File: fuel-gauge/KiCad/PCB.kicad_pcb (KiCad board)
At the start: 2 copper layers, 100 x 70 mm, 39 parts, among them P1 CONN_01X04, P2 CONN_01X04, P3 CONN_01X04, Q1 BSS84, Q2 BSS138, Q3 2N7002, SW1 Switch_SPDT_x2, U1 AQV252G, U2 SN74LVC1G08DBVR, U3 TLV3691IDCKR, U4 bq34z100pw

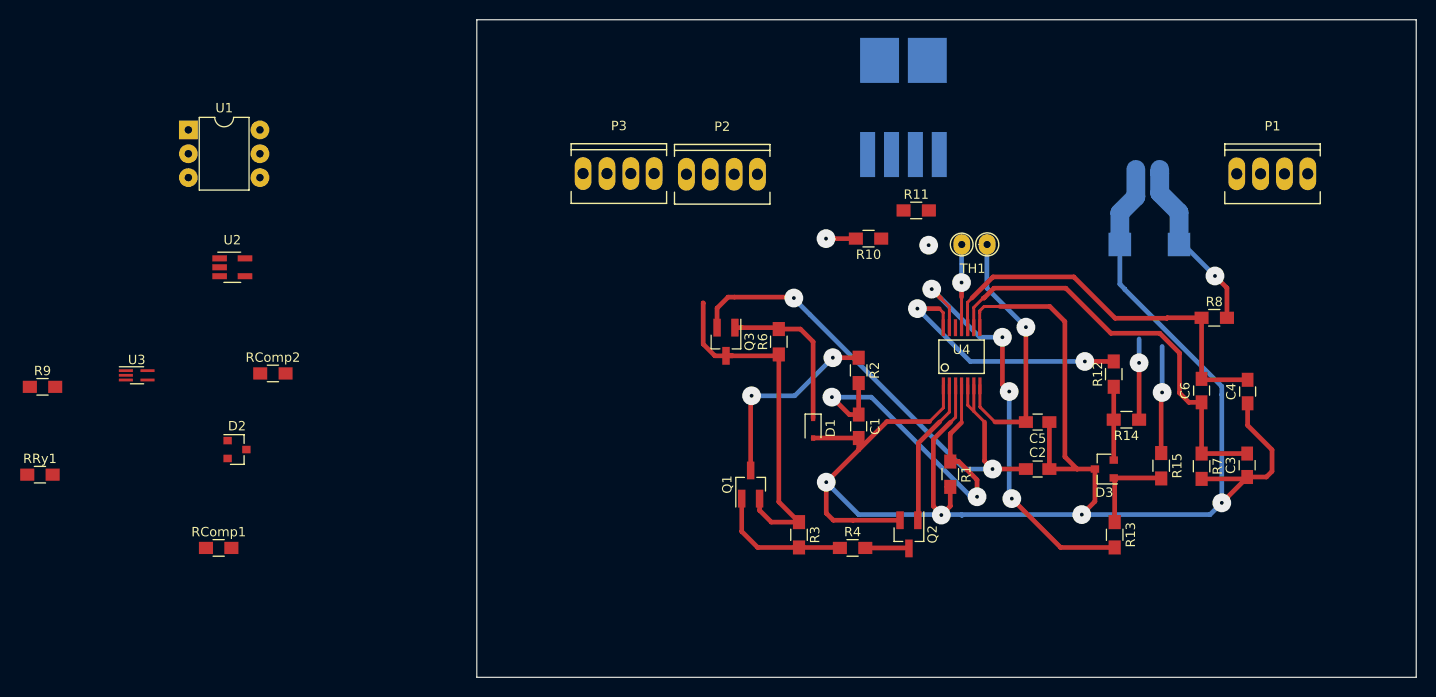
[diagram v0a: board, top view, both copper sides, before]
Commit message: Update fuel gauge pcb design to the v2
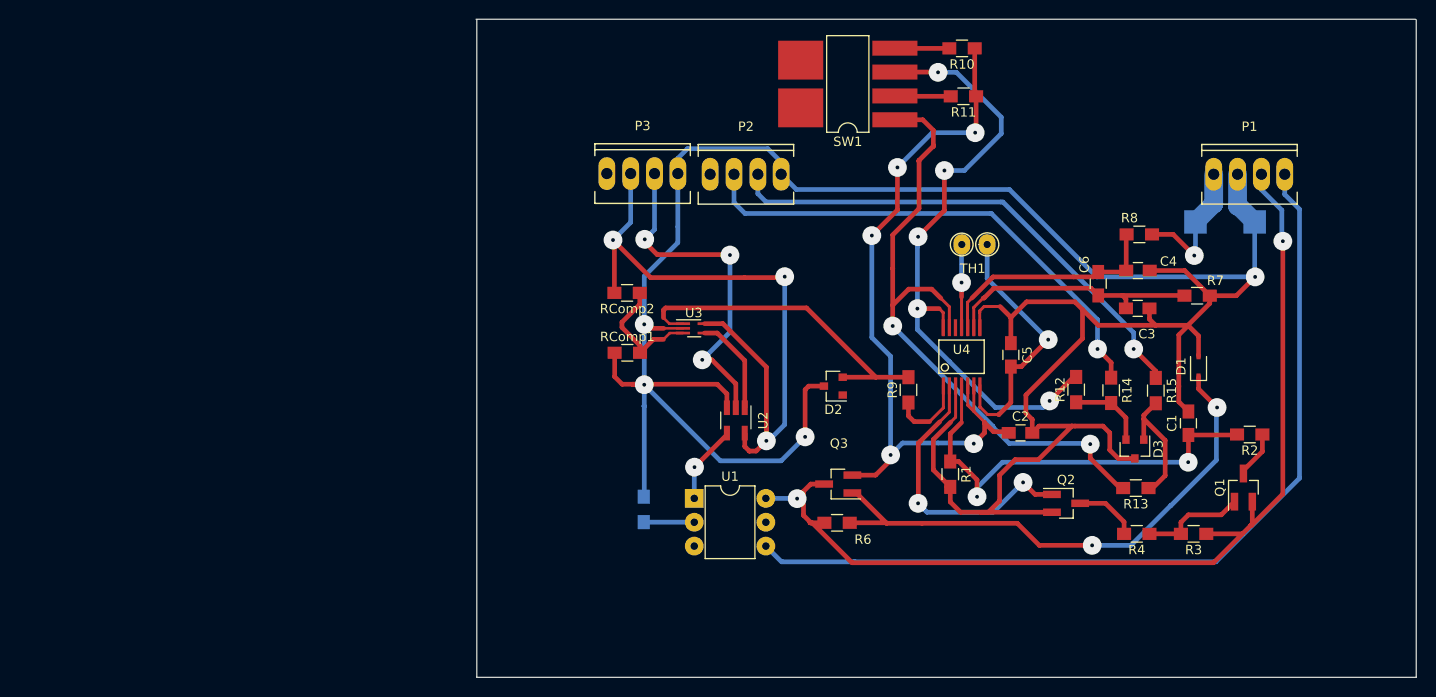
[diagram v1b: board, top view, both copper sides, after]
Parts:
- RRy1: moved to B.Cu
- SW1: moved to F.Cu
- moved R9 92.2 mm to (145.9, 99.4), turned to 90 degrees
- moved U1 66.6 mm to (123.2, 111.0)
- moved RRy1 64.4 mm to (117.8, 112.1), turned to 270 degrees
- moved D2 63.8 mm to (137.9, 99.0), turned to 180 degrees
- moved U3 59.5 mm to (123.1, 93.1)
- moved U2 56.0 mm to (127.6, 102.7), turned to 270 degrees
- moved Q1 52.5 mm to (181.6, 109.8)
- moved RComp1 48.2 mm to (116.0, 95.5)
- moved R2 42.2 mm to (182.3, 104.2), turned to 180 degrees
- moved R3 42.0 mm to (176.3, 114.7), turned to 180 degrees
- moved D1 41.5 mm to (176.8, 96.9), turned to 90 degrees
- moved RComp2 38.7 mm to (116.0, 89.1), turned to 180 degrees
- moved C1 35.1 mm to (175.8, 103.0), turned to 90 degrees
- moved R4 30.3 mm to (170.2, 114.7), turned to 180 degrees
- moved R10 22.6 mm to (151.7, 63.0)
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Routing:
- net GNDREF: track 92.3 -> 302.6 mm, vias 0 -> 4
- net Net-(R9-Pad1): track 112.2 -> 8.58 mm, vias 4 -> 0
- net /PUSHBUTTON: track 0.00 -> 94.3 mm
- net +5V: track 0.00 -> 73.1 mm, vias 0 -> 3
- net /BATT+: track 38.4 -> 110.2 mm, vias 0 -> 2
- net /SDA: track 8.80 -> 53.6 mm
- net /SCL: track 11.6 -> 54.0 mm
- net Net-(D1-Pad1): track 17.1 -> 58.6 mm, vias 0 -> 2
- net Net-(R12-Pad2): track 28.5 -> 67.9 mm, vias 2 -> 5
- net Net-(P3-Pad3): track 0.00 -> 36.9 mm, vias 0 -> 3
- net Net-(D2-Pad1): track 0.00 -> 35.9 mm
- net Net-(R13-Pad2): track 45.9 -> 70.3 mm, vias 4 -> 2
- net REG_IN: track 56.2 -> 79.5 mm, vias 2 -> 5
- net Net-(C3-Pad2): track 45.9 -> 28.1 mm
- net Net-(C4-Pad2): track 43.0 -> 25.7 mm
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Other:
- board size 100 x 70 mm -> 100.1 x 70 mm
- rule trace_min: 0.32 -> 0.28

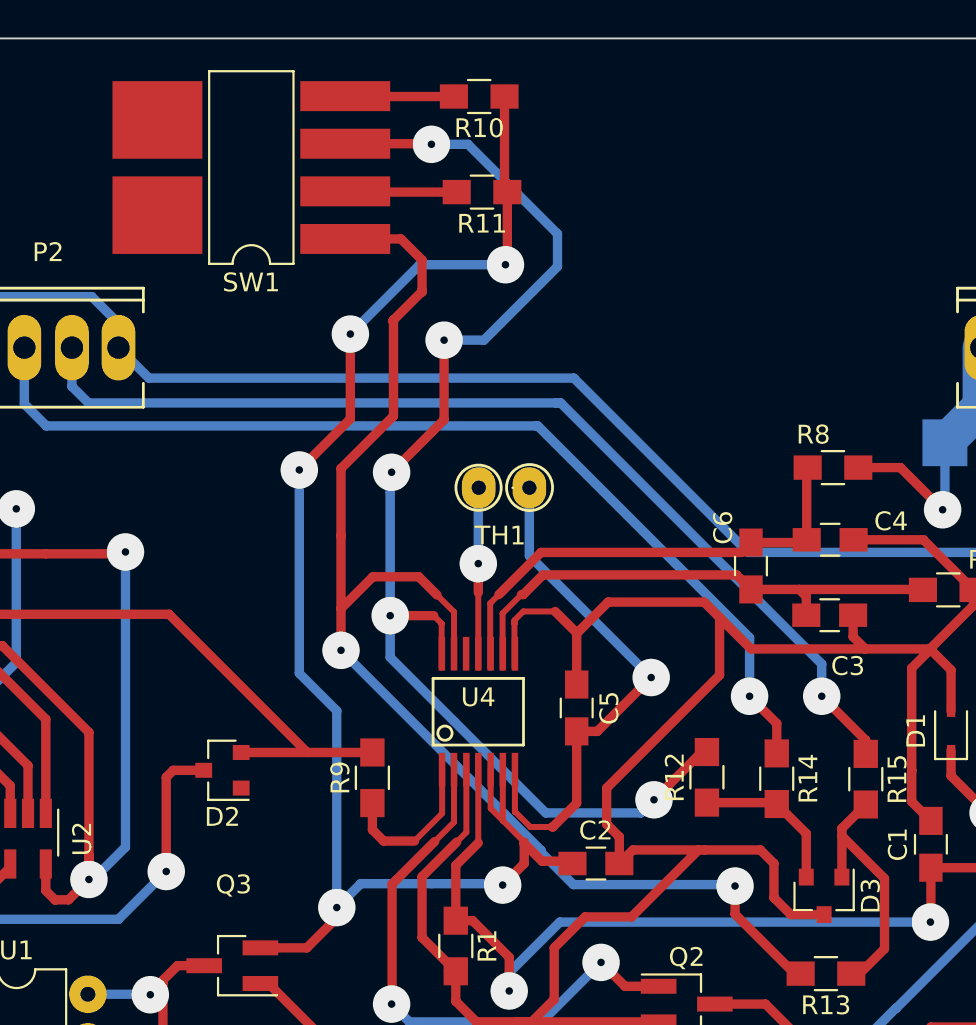
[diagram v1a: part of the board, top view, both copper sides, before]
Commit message: Switch moved because of the proximity to the connector.
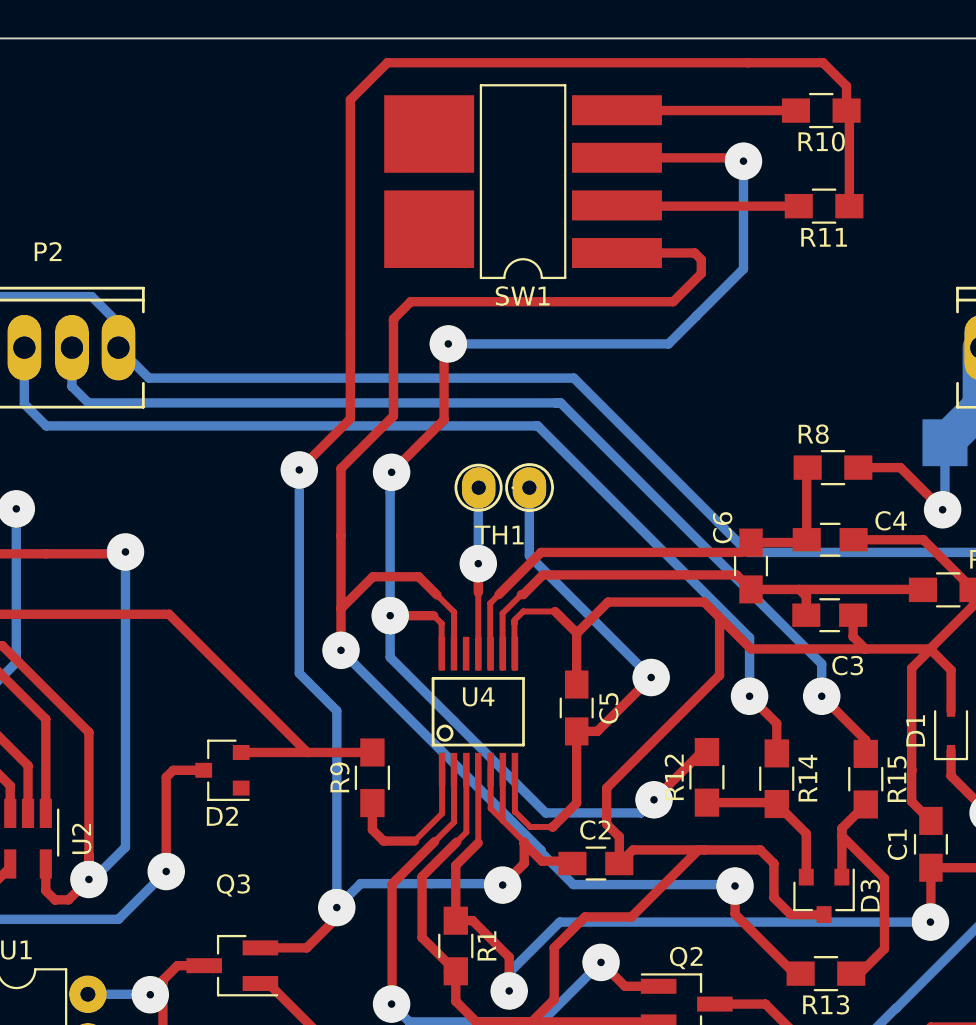
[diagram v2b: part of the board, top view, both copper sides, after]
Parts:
- moved R10 18.3 mm to (169.9, 63.8)
- moved R11 18.3 mm to (170.1, 68.9)
- moved SW1 14.5 mm to (157.8, 71.4)
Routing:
- net REG_IN: track 79.5 -> 107.8 mm, vias 5 -> 3
- net Net-(R13-Pad2): track 70.3 -> 84.6 mm
- net Net-(R12-Pad2): track 67.9 -> 75.0 mm
- net Net-(R11-Pad2): track 5.97 -> 9.77 mm
- net Net-(R10-Pad2): track 5.81 -> 9.59 mm
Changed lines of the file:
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@@
-(kicad_pcb (version 4) (host pcbnew 4.0.0-rc2-stable)
+(kicad_pcb (version 4) (host pcbnew 4.0.6)
   (general
     (links 76)
     (no_connects 0)
-    (area 94.899999 49.899999 218.428572 144.700001)
+    (area 99.874999 59.899999 200.050001 130.050001)
     (thickness 1.6)
     (drawings 17)
-    (tracks 457)
+    (tracks 460)
     (zones 0)
     (modules 39)
@@
   )
   (module myfootprint:R_0805_My_HandSoldering (layer F.Cu)
-    (at 151.65 63.05 180)
+    (at 169.9 63.8 180)
     (descr "Resistor SMD 0805, hand soldering")
     (tags "resistor 0805")
@@
   )
   (module myfootprint:R_0805_My_HandSoldering (layer F.Cu)
-    (at 151.8 68.15 180)
+    (at 170.05 68.9 180)
     (descr "Resistor SMD 0805, hand soldering")
     (tags "resistor 0805")
@@
   )
   (module footprint:SW1-DIP-8-_6_Handsoldering (layer F.Cu)
-    (at 143.3 70.65 180)
+    (at 157.8 71.4 180)
     (descr "8-lead though-hole mounted DIP package, row spacing 7.62 mm (300 mils), LongPads")
     (tags "THT DIP DIL PDIP 2.54mm 7.62mm 300mil LongPads")
@@
   (segment (start 150.4 104.075) (end 151.6 102.875) (width 0.5) (layer F.Cu) (net 1))
   (segment (start 150.4 107.025) (end 150.4 107.025) (width 0.5) (layer F.Cu) (net 1) (status 30))
+  (segment (start 171.4 68.9) (end 171.4 63.95) (width 0.5) (layer F.Cu) (net 2) (status C00000))
+  (segment (start 171.4 63.95) (end 171.25 63.8) (width 0.5) (layer F.Cu) (net 2) (status C00000))
+  (segment (start 166 61.25) (end 170 61.25) (width 0.5) (layer F.Cu) (net 2))
+  (segment (start 144.775 63.225) (end 146.75 61.25) (width 0.5) (layer F.Cu) (net 2))
+  (segment (start 146.75 61.25) (end 166 61.25) (width 0.5) (layer F.Cu) (net 2))
   (segment (start 144.775 75.725) (end 144.775 80.25) (width 0.5) (layer F.Cu) (net 2))
-  (segment (start 144.05 95.825) (end 144.05 106.325) (width 0.5) (layer B.Cu) (net 2))
+  (segment (start 144.05 106.325) (end 144.05 95.825) (width 0.5) (layer B.Cu) (net 2))
   (via (at 142.05 82.975) (size 2) (drill 0.4) (layers F.Cu B.Cu) (net 2))
   (segment (start 142.05 93.825) (end 142.05 82.975) (width 0.5) (layer B.Cu) (net 2))
   (segment (start 144.05 95.825) (end 142.05 93.825) (width 0.5) (layer B.Cu) (net 2))
   (segment (start 144.775 80.25) (end 142.05 82.975) (width 0.5) (layer F.Cu) (net 2))
-  (segment (start 153.15 71.925) (end 153.15 68.15) (width 0.5) (layer F.Cu) (net 2))
-  (segment (start 153.05 72.025) (end 153.15 71.925) (width 0.5) (layer F.Cu) (net 2))
-  (via (at 153.05 72.025) (size 2) (drill 0.4) (layers F.Cu B.Cu) (net 2))
-  (segment (start 148.475 72.025) (end 153.05 72.025) (width 0.5) (layer B.Cu) (net 2))
-  (segment (start 144.775 75.725) (end 148.475 72.025) (width 0.5) (layer B.Cu) (net 2))
-  (via (at 144.775 75.725) (size 2) (drill 0.4) (layers F.Cu B.Cu) (net 2))
-  (segment (start 144.8 75.75) (end 144.775 75.725) (width 0.5) (layer F.Cu) (net 2))
-  (segment (start 153 63.05) (end 153 68) (width 0.5) (layer F.Cu) (net 2))
-  (segment (start 153 68) (end 153.15 68.15) (width 0.5) (layer F.Cu) (net 2))
+  (segment (start 144.775 75.725) (end 144.775 63.225) (width 0.5) (layer F.Cu) (net 2))
+  (segment (start 171.25 62.5) (end 171.25 63.8) (width 0.5) (layer F.Cu) (net 2) (status 800000))
+  (segment (start 170 61.25) (end 171.25 62.5) (width 0.5) (layer F.Cu) (net 2))
+  (segment (start 171.4 63.95) (end 171.25 63.8) (width 0.5) (layer F.Cu) (net 2))
+  (segment (start 171.25 68.75) (end 171.4 68.9) (width 0.5) (layer F.Cu) (net 2))
   (segment (start 139.975 108.475) (end 142.45 108.475) (width 0.5) (layer F.Cu) (net 2))
   (segment (start 142.45 108.475) (end 144.05 106.875) (width 0.5) (layer F.Cu) (net 2))
@@
   (segment (start 151.6 89.525) (end 151.6 93.531) (width 0.32) (layer F.Cu) (net 17))
   (via (at 151.6 87.975) (size 2) (drill 0.4) (layers F.Cu B.Cu) (net 17))
-  (segment (start 149.775 76.05) (end 149.775 80.3) (width 0.5) (layer F.Cu) (net 18))
-  (segment (start 146.9 84.175) (end 146.9 90.75) (width 0.5) (layer B.Cu) (net 18))
+  (segment (start 163.25 74.75) (end 165.75 72.25) (width 0.5) (layer B.Cu) (net 18))
+  (segment (start 149.775 76.475) (end 150 76.25) (width 0.5) (layer F.Cu) (net 18))
+  (via (at 150 76.25) (size 2) (drill 0.4) (layers F.Cu B.Cu) (net 18))
+  (segment (start 150 76.25) (end 161.75 76.25) (width 0.5) (layer B.Cu) (net 18))
+  (segment (start 161.75 76.25) (end 163.25 74.75) (width 0.5) (layer B.Cu) (net 18))
+  (segment (start 146.9 90.75) (end 146.9 84.175) (width 0.5) (layer B.Cu) (net 18))
   (segment (start 146.9 83.175) (end 146.9 84.175) (width 0.5) (layer B.Cu) (net 18))
   (segment (start 146.975 83.1) (end 146.9 83.175) (width 0.5) (layer B.Cu) (net 18))
   (via (at 146.975 83.1) (size 2) (drill 0.4) (layers F.Cu B.Cu) (net 18))
   (segment (start 149.775 80.3) (end 146.975 83.1) (width 0.5) (layer F.Cu) (net 18))
-  (segment (start 149.775 76.05) (end 151.9 76.05) (width 0.5) (layer B.Cu) (net 18))
-  (via (at 149.775 76.05) (size 2) (drill 0.4) (layers F.Cu B.Cu) (net 18))
-  (segment (start 149.775 76.05) (end 149.725 76.1) (width 0.5) (layer F.Cu) (net 18))
-  (segment (start 149.07 65.57) (end 144.5 65.57) (width 0.5) (layer F.Cu) (net 18))
-  (segment (start 149.1 65.6) (end 149.07 65.57) (width 0.5) (layer F.Cu) (net 18))
-  (via (at 149.1 65.6) (size 2) (drill 0.4) (layers F.Cu B.Cu) (net 18))
-  (segment (start 151.05 65.6) (end 149.1 65.6) (width 0.5) (layer B.Cu) (net 18))
-  (segment (start 155.825 70.375) (end 151.05 65.6) (width 0.5) (layer B.Cu) (net 18))
-  (segment (start 155.825 72.125) (end 155.825 70.375) (width 0.5) (layer B.Cu) (net 18))
-  (segment (start 151.9 76.05) (end 155.825 72.125) (width 0.5) (layer B.Cu) (net 18))
+  (segment (start 149.775 80.3) (end 149.775 76.475) (width 0.5) (layer F.Cu) (net 18))
+  (segment (start 165.57 66.32) (end 159 66.32) (width 0.5) (layer F.Cu) (net 18) (status 800000))
+  (segment (start 165.75 66.5) (end 165.57 66.32) (width 0.5) (layer F.Cu) (net 18))
+  (via (at 165.75 66.5) (size 2) (drill 0.4) (layers F.Cu B.Cu) (net 18))
+  (segment (start 165.75 72.25) (end 165.75 66.5) (width 0.5) (layer B.Cu) (net 18))
   (segment (start 155.2 101.275) (end 160.275 101.275) (width 0.5) (layer B.Cu) (net 18))
   (segment (start 160.275 101.275) (end 160.975 100.575) (width 0.5) (layer B.Cu) (net 18))
@@
   (segment (start 149.6442 93.531) (end 149.6442 91.1808) (width 0.32) (layer F.Cu) (net 18))
   (segment (start 149.6442 91.1808) (end 149.6442 91.1692) (width 0.32) (layer F.Cu) (net 18))
+  (segment (start 147.075 75) (end 147.075 74.925) (width 0.5) (layer F.Cu) (net 19))
+  (segment (start 163.15 71.4) (end 159 71.4) (width 0.5) (layer F.Cu) (net 19))
+  (segment (start 163.5 71.75) (end 163.15 71.4) (width 0.5) (layer F.Cu) (net 19))
+  (segment (start 163.5 72.5) (end 163.5 71.75) (width 0.5) (layer F.Cu) (net 19))
+  (segment (start 162 74) (end 163.5 72.5) (width 0.5) (layer F.Cu) (net 19))
+  (segment (start 148 74) (end 162 74) (width 0.5) (layer F.Cu) (net 19))
+  (segment (start 147.075 74.925) (end 148 74) (width 0.5) (layer F.Cu) (net 19))
   (segment (start 144.275 86.5) (end 144.275 82.9) (width 0.5) (layer F.Cu) (net 19))
-  (segment (start 147.075 80.1) (end 147.075 74.975) (width 0.5) (layer F.Cu) (net 19))
+  (segment (start 147.075 80.1) (end 147.075 75) (width 0.5) (layer F.Cu) (net 19))
+  (segment (start 147.075 75) (end 147.075 74.975) (width 0.5) (layer F.Cu) (net 19))
   (segment (start 144.275 82.9) (end 147.075 80.1) (width 0.5) (layer F.Cu) (net 19))
-  (segment (start 148.6 73.375) (end 148.6 73.45) (width 0.5) (layer F.Cu) (net 19))
-  (segment (start 148.6 73.45) (end 147.075 74.975) (width 0.5) (layer F.Cu) (net 19))
   (segment (start 144.275 86.475) (end 144.275 86.5) (width 0.5) (layer F.Cu) (net 19))
   (segment (start 144.275 86.5) (end 144.275 90.375) (width 0.5) (layer F.Cu) (net 19))
-  (segment (start 147.075 74.975) (end 147.025 75.025) (width 0.5) (layer F.Cu) (net 19))
-  (segment (start 147.475 70.65) (end 148.6 71.775) (width 0.5) (layer F.Cu) (net 19))
-  (segment (start 148.6 71.775) (end 148.6 73.375) (width 0.5) (layer F.Cu) (net 19))
-  (segment (start 148.6 73.375) (end 148.6 73.5) (width 0.5) (layer F.Cu) (net 19))
-  (segment (start 147.475 70.65) (end 144.5 70.65) (width 0.5) (layer F.Cu) (net 19))
   (segment (start 168.8 109.85) (end 168.475 109.85) (width 0.5) (layer F.Cu) (net 19))
   (segment (start 168.475 109.85) (end 165.3 106.675) (width 0.5) (layer F.Cu) (net 19))
@@
   (segment (start 125.6 93.35) (end 124.25 93.35) (width 0.5) (layer F.Cu) (net 28))
   (segment (start 128.525 96.275) (end 125.6 93.35) (width 0.5) (layer F.Cu) (net 28))
-  (segment (start 150.3 63.05) (end 144.52 63.05) (width 0.5) (layer F.Cu) (net 29))
-  (segment (start 144.52 63.05) (end 144.5 63.03) (width 0.5) (layer F.Cu) (net 29))
-  (segment (start 150.45 68.15) (end 144.54 68.15) (width 0.5) (layer F.Cu) (net 30))
-  (segment (start 144.54 68.15) (end 144.5 68.11) (width 0.5) (layer F.Cu) (net 30))
+  (segment (start 168.55 63.8) (end 159.02 63.8) (width 0.5) (layer F.Cu) (net 29) (status C00000))
+  (segment (start 159.02 63.8) (end 159 63.78) (width 0.5) (layer F.Cu) (net 29) (status C00000))
+  (segment (start 159.02 63.8) (end 159 63.78) (width 0.5) (layer F.Cu) (net 29))
+  (segment (start 168.7 68.9) (end 159.04 68.9) (width 0.5) (layer F.Cu) (net 30) (status C00000))
+  (segment (start 159.04 68.9) (end 159 68.86) (width 0.5) (layer F.Cu) (net 30) (status C00000))
+  (segment (start 159.04 68.9) (end 159 68.86) (width 0.5) (layer F.Cu) (net 30))
   (segment (start 136.95 99) (end 135.325 99) (width 0.5) (layer F.Cu) (net 31))
   (segment (start 125.925 106.95) (end 117.825 98.85) (width 0.5) (layer B.Cu) (net 31))
